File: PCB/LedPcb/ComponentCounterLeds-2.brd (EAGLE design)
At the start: 50 x 20.5 mm, 13 parts

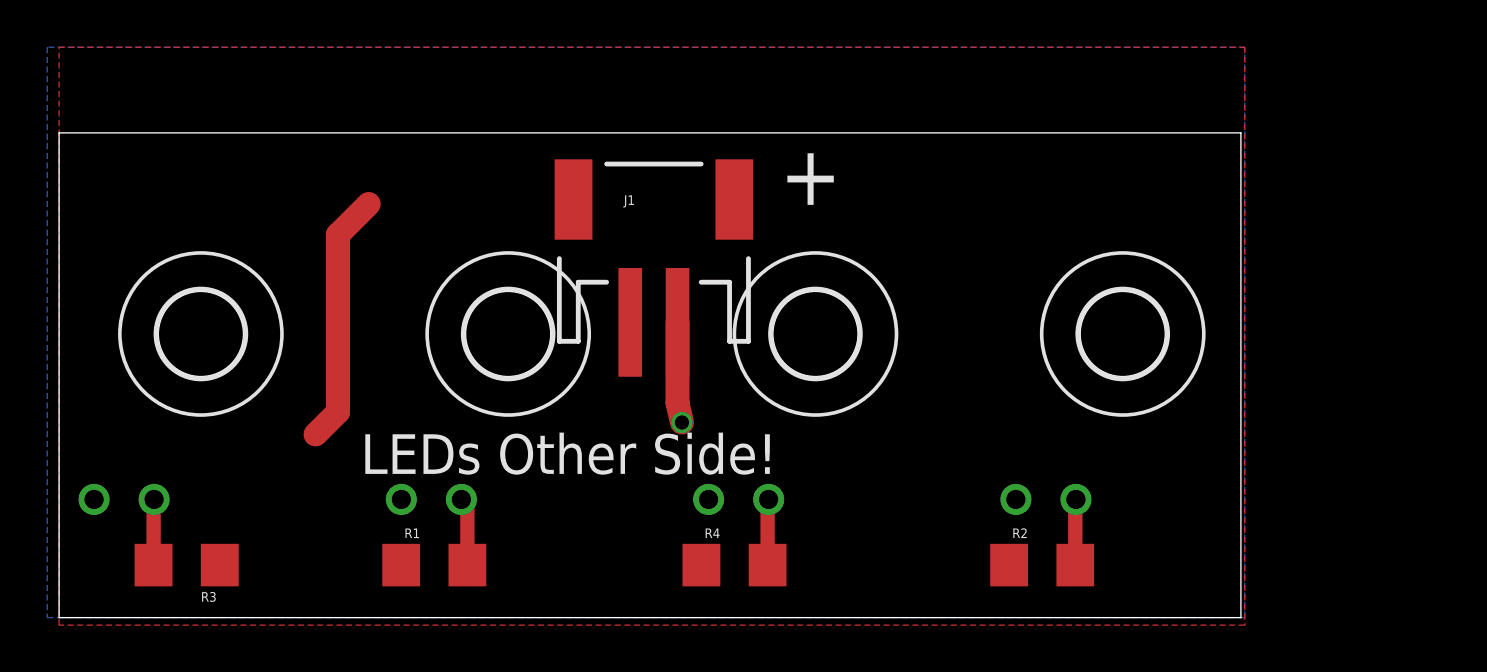
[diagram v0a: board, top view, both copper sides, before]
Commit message: Changed each spool block width to 15mm to give more space for the spools.
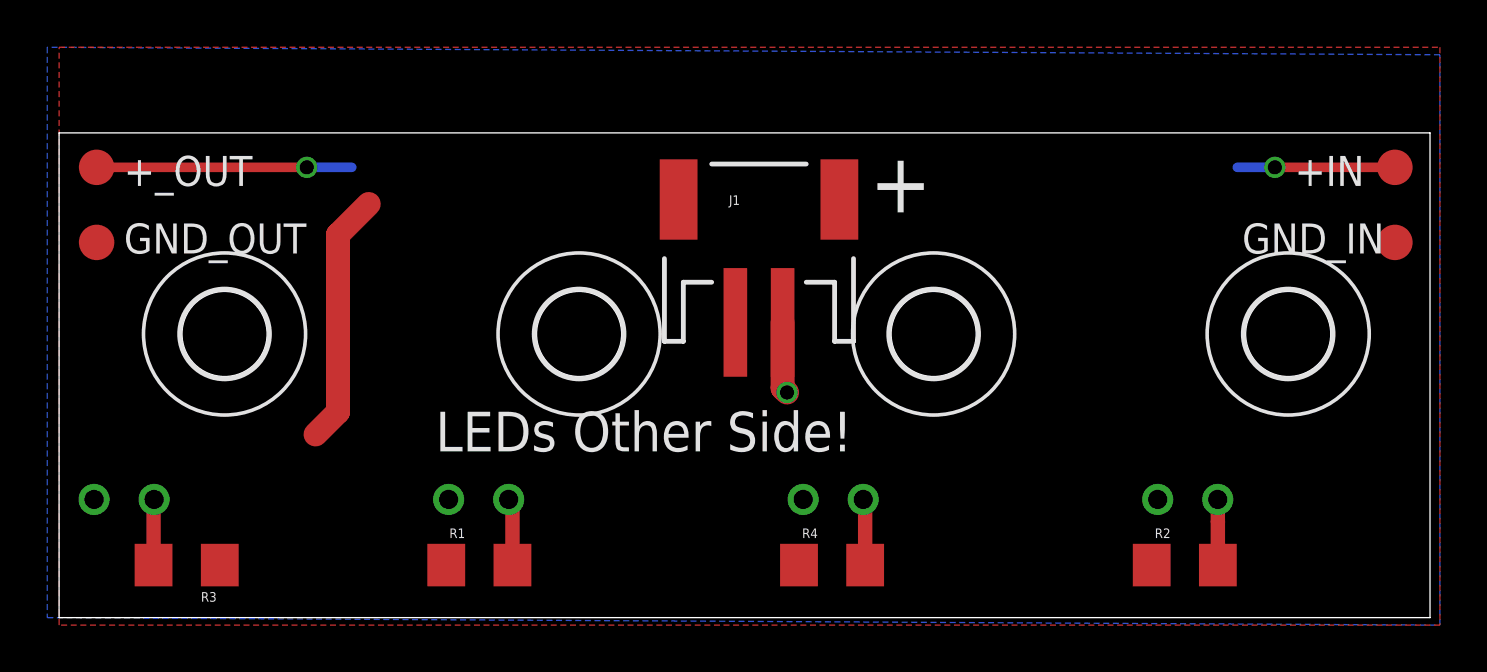
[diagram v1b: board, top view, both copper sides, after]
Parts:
- added +IN, +_OUT, GND_IN, GND_OUT: TPTP15R, testpad:TP15R
- moved H4 7.00 mm to (52.0, 12.0)
- moved R2 6.03 mm to (47.6, 2.22)
- moved D4 6.00 mm to (47.8, 5.00)
- moved H3 5.00 mm to (37.0, 12.0)
- moved J1 4.45 mm to (29.6, 16.2)
- moved R4 4.13 mm to (32.7, 2.22)
- moved D3 4.00 mm to (32.8, 5.00)
- moved H2 3.00 mm to (22.0, 12.0)
- moved D2 2.00 mm to (17.8, 5.00)
- moved R1 1.91 mm to (17.8, 2.22)
- moved H1 1.00 mm to (7.00, 12.0)
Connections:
- net 5V: now also +IN.TP, +_OUT.TP
- net GND: now also GND_IN.TP, GND_OUT.TP
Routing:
- net 5V: track 4.26 -> 20.5 mm, vias 1 -> 3
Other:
- board size 50 x 20.5 mm -> 58 x 20.5 mm
